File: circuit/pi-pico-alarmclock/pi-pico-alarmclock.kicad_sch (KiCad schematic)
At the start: 33 parts, among them J1 Screw_Terminal_2_P5.00mm, J2 BTN GREEN, J3 BTN BLUE, J4 BTN_YELLOW, J5 NEOPIXEL, J6 OLED, J7 BAT - Screw_Terminal_2_P5.00mm, Q1 IRLZ44N, Q3 IRF9540, Q4 IRLZ44N, U1 Pico, U3 TC4056A Charger Module

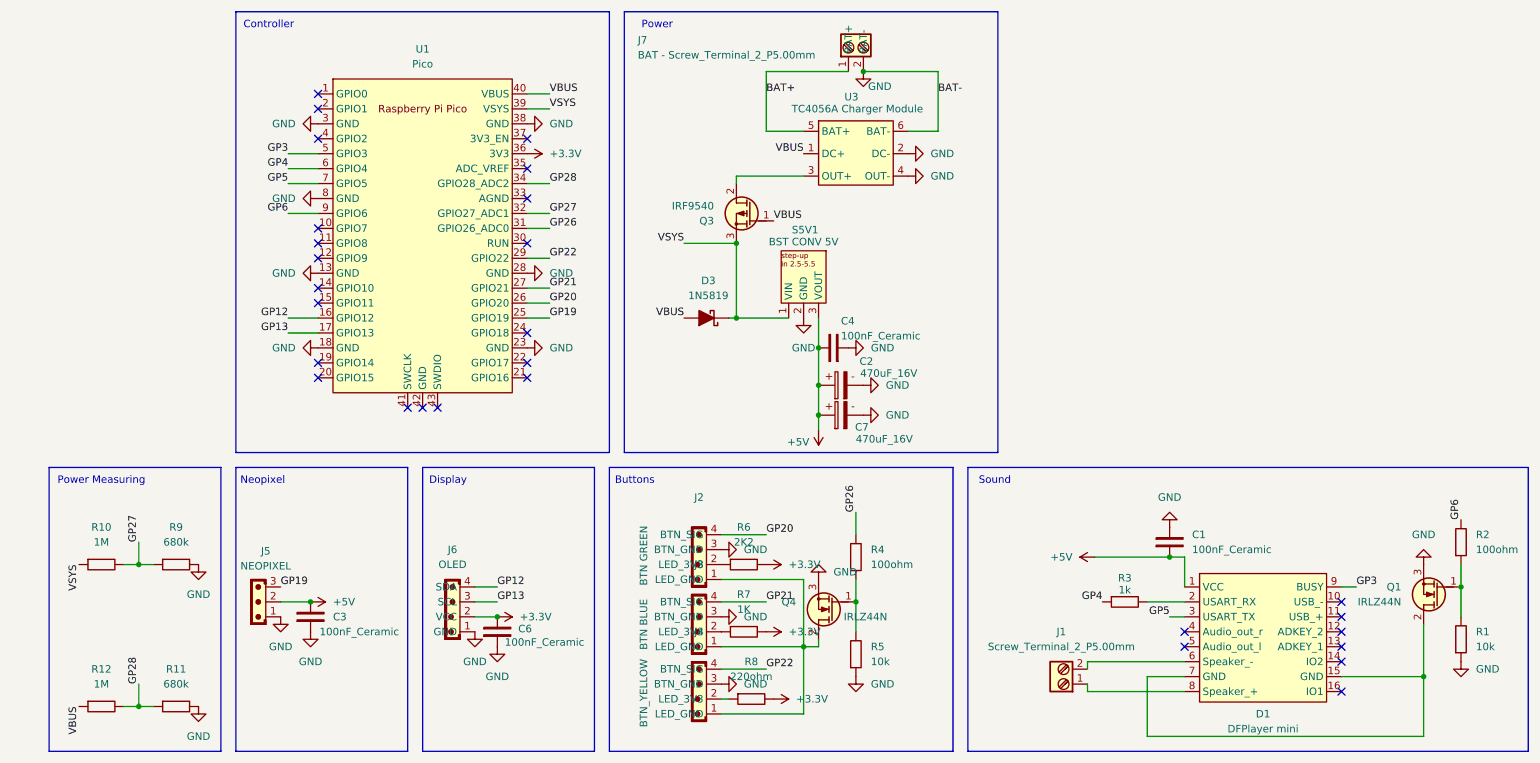
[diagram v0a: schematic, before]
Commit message: Things found while real life testing (#79)
* Add noise filtering for power detection

Use median filtering for VSYS readings, debounce VBUS, and add 0.1V
hysteresis to suppress display flicker. Add moving_median dependency and
document the strategy in README

* Do not stop sound on standby, fixes race condition after going out of
standby

* Issue with not playing sound after standby and after alarms that had
quit by the end of the song: Race of pending sound stop signal. Solution
is to track DFPlayer power state and gate stop signal to only when it is
even powered.

* Add ClockTime and avoid redundant LED writes

* Bump version to 0.7.2 and add lessons learned

* Use PIN_15 for WS2812 instead of PIN_19

* Add Neopixel power control and state handle

Use PIN_14 to control Neopixel power and pass an explicit NeopixelHandle
through effects. Ensure proper power-on/off sequencing with small delays
and update alarm brightness default to 7.

* Initialize Neopixel in main and pass to task

* Move Neopixel control pin from GPIO19 to GPIO15, introduce power
management for Neopixel via GPIO14 and another IRLZ44N.

* Reduce divider impedance and update ADC scaling

Lower impedance voltage dividers and add decoupling/filter caps:
- R9,R11: 680k -> 100k; R10,R12: 1M -> 200k
- Add R14 and R13 grouping changes to resistor table
- Add C5 and ADC filter caps C8,C9; update capacitor table Update power
  reader to use divider ratio 3.0 (was 2.47) and revise README
  noise-filtering text accordingly

* Correct GPIO nets, update placements and values

Rename GPIO nets (GP14/GP15/GP19) and Q2 nets; adjust pad pintypes.
Reposition multiple footprints and update silk/fab layers. Change
resistor values (1M -> 200K, 680k -> 100K). Add PCB .stl step file, plus
GND symbols and a 100nF decoupling cap.

* Update src/task/power.rs

Co-authored-by: Copilot <175728472+Copilot@users.noreply.github.com>

* Update README.md

Co-authored-by: Copilot <175728472+Copilot@users.noreply.github.com>

* Update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
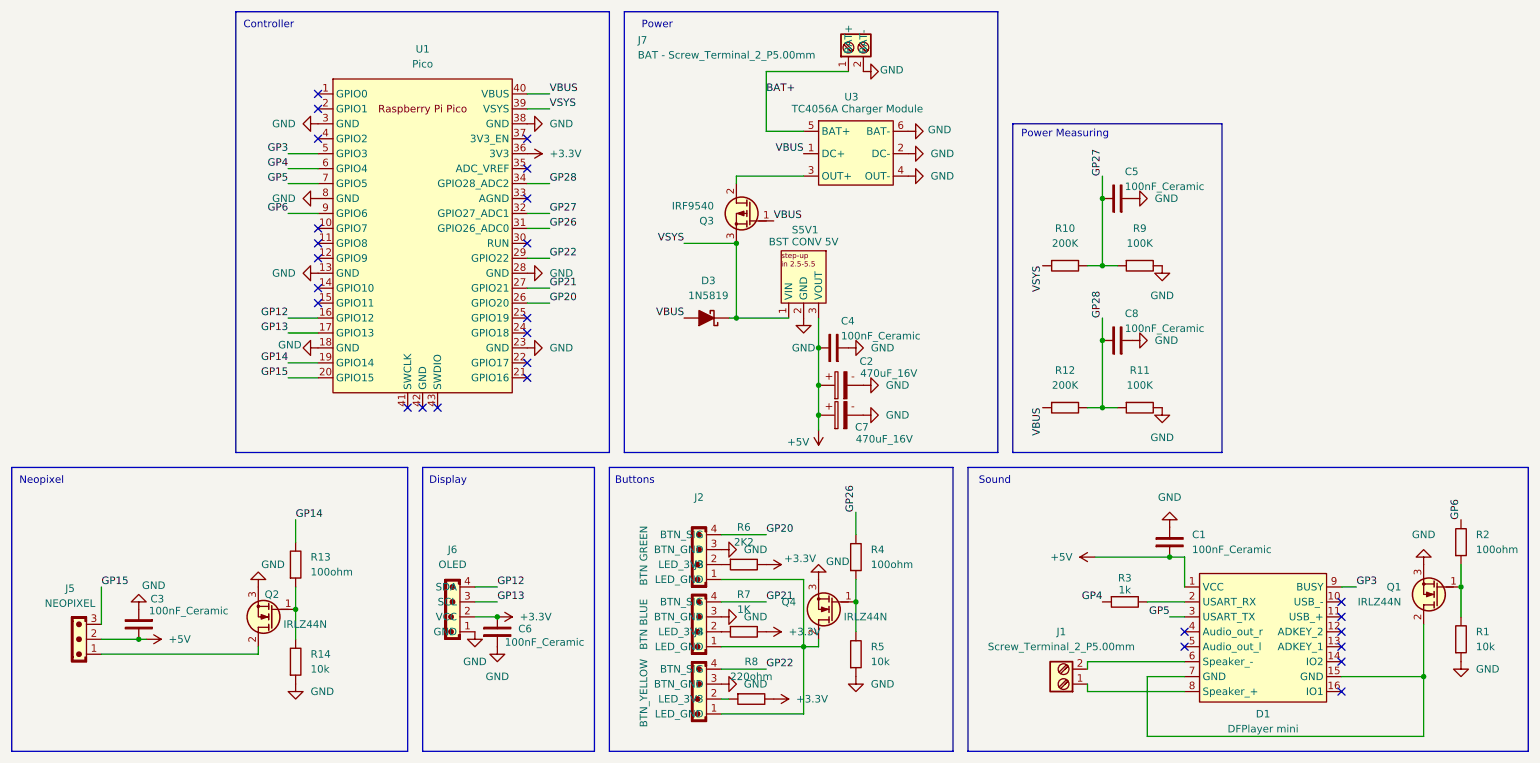
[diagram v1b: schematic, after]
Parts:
- added C5, C8: 100nF_Ceramic, Capacitor_THT:C_Disc_D5.0mm_W2.5mm_P2.50mm, symbol PCM_SL_Capacitors:100nF_Ceramic
- added Q2: IRLZ44N, PCM_Package_TO_SOT_THT_AKL:TO-220-3_Vertical_GDS, symbol PCM_Transistor_MOSFET_AKL:IRLZ44N
- added R13: 100ohm, Resistor_THT:R_Axial_DIN0207_L6.3mm_D2.5mm_P10.16mm_Horizontal, symbol PCM_SL_Resistors:100ohm
- added R14: 10k, Resistor_THT:R_Axial_DIN0207_L6.3mm_D2.5mm_P10.16mm_Horizontal, symbol PCM_SL_Resistors:10k
- R10, R12: value 1M -> 200K
- R11, R9: value 680k -> 100K
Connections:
- net GND: now also C5.1, C8.1, Q2.3 (S), R14.1; no longer J5.1
- net GP27: now also C5.2
- net GP28: now also C8.2
- net GP14: now reaches U1.19 (GPIO14)
- net GP14: now also R13.2
- net GP15: now reaches U1.20 (GPIO15)
- net GP15: now also J5.3
- net GP19: no longer names the net of U1.25 (GPIO19)
- net GP19: no longer J5.3
- new net: J5.1, Q2.2 (D)
- new net: Q2.1 (G), R13.1, R14.2
- no-connect marks 28 -> 27
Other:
- moved on the sheet: C3, J5, R10, R11, R12, R9
